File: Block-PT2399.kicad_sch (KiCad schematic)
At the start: 24 parts, among them J1 Sig_in, J2 Sig_out, J3 Sig_gnd, J4 +9V, Q1 2N3819, U1 LM7805_TO220, U2 PT2399

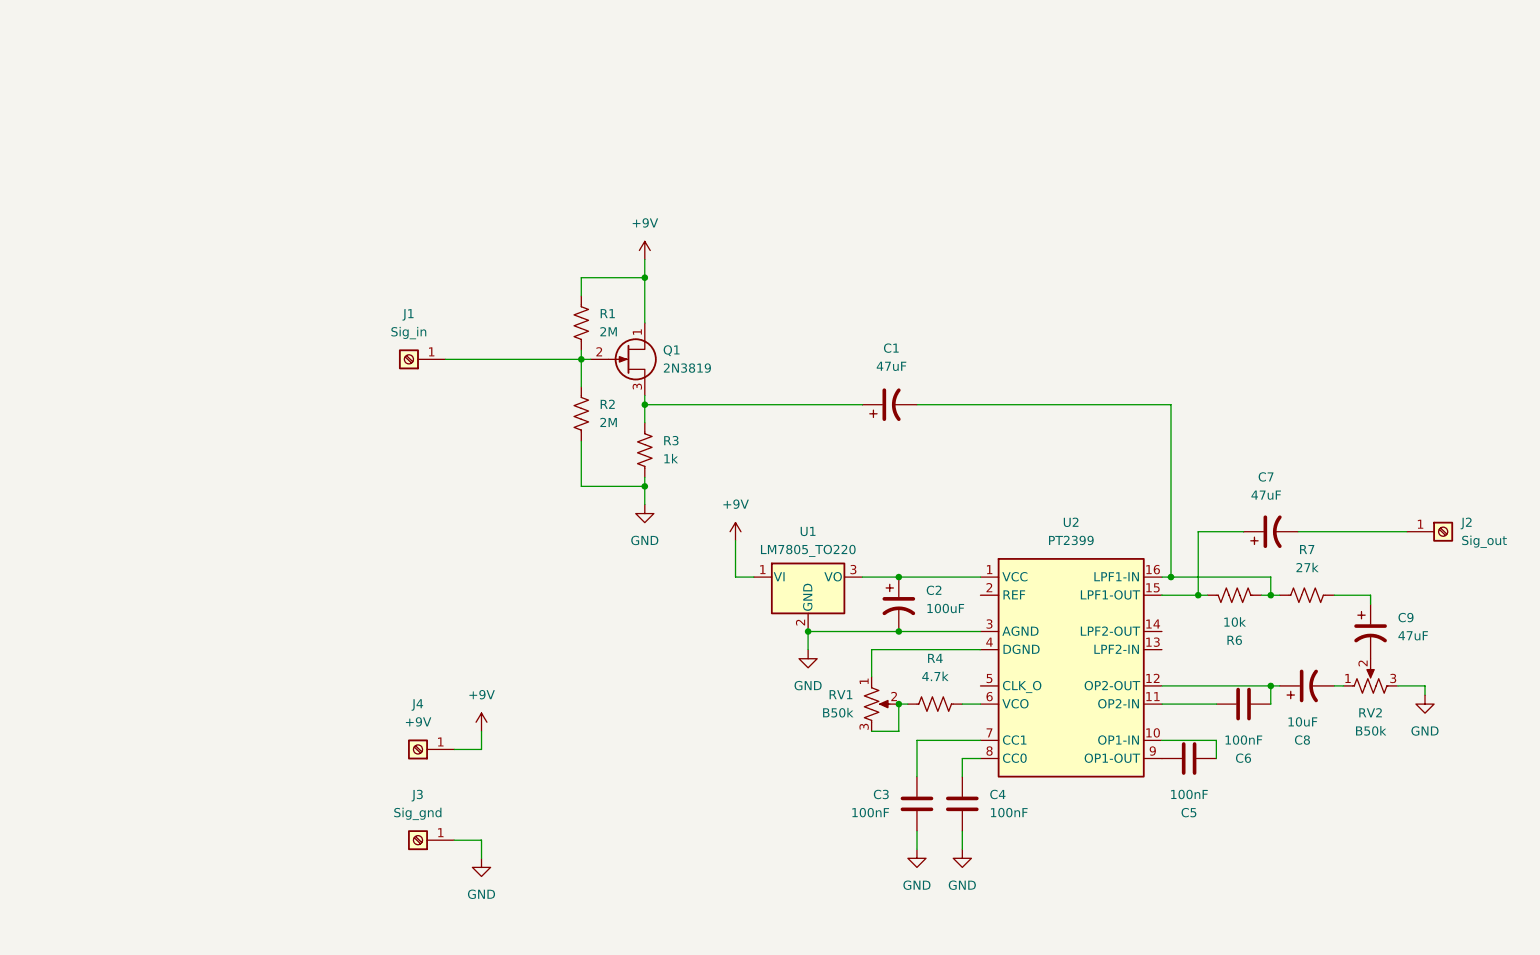
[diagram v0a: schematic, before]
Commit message: implement pin-2 hack and anti-latch
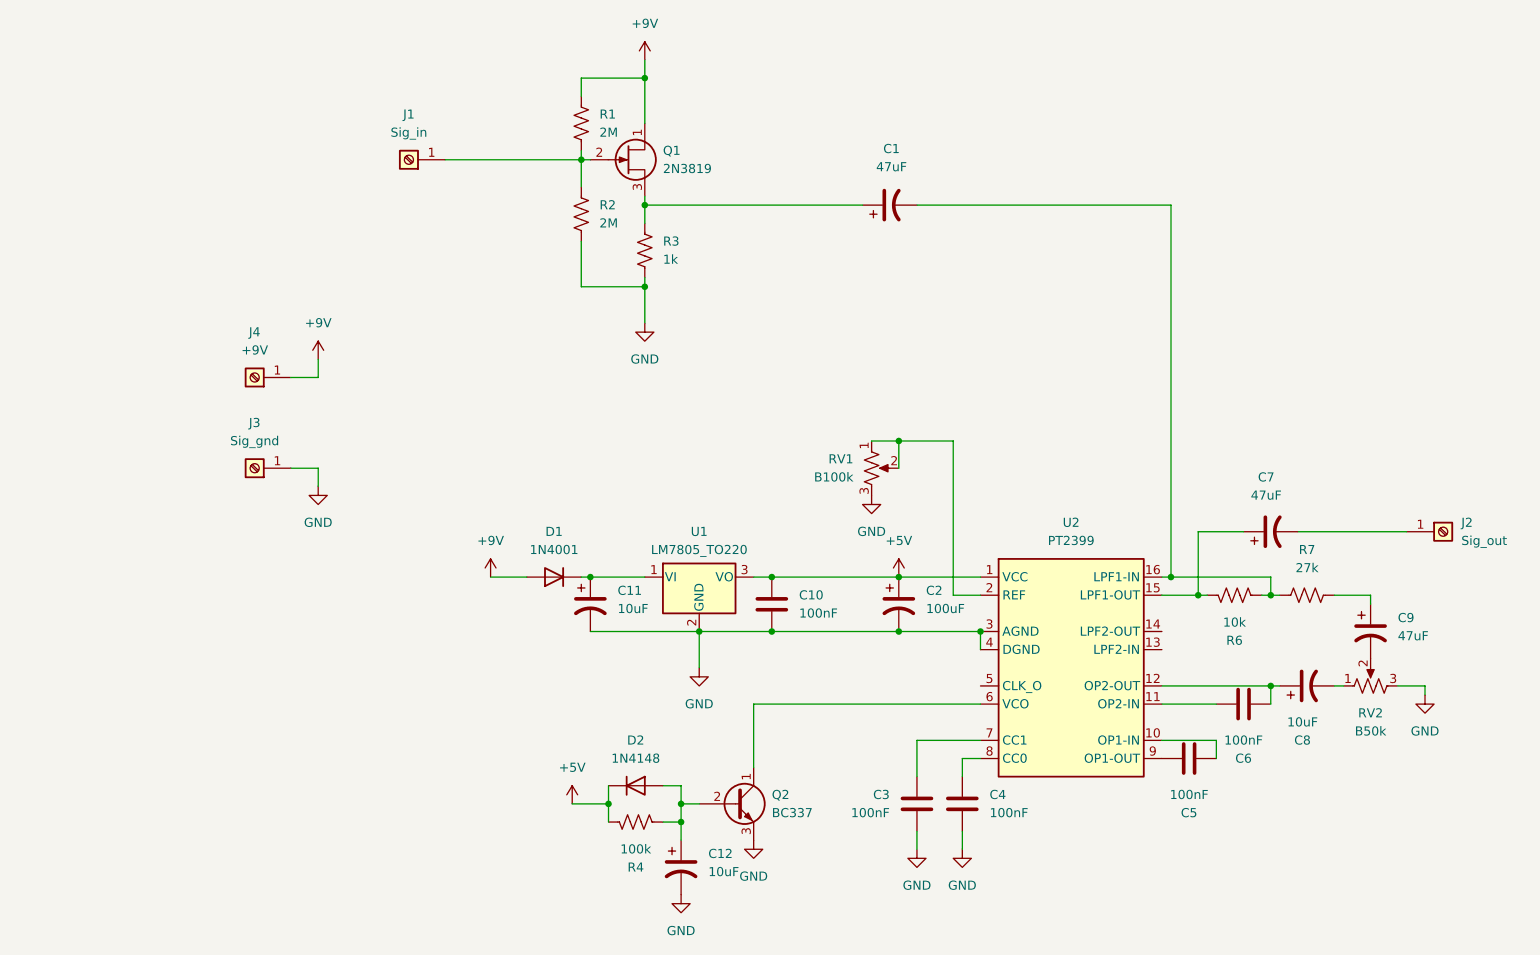
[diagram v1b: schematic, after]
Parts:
- added C10: 100nF, Capacitor_THT:C_Disc_D3.0mm_W1.6mm_P2.50mm, symbol Device:C
- added C11: 10uF, Capacitor_THT:CP_Radial_D5.0mm_P2.00mm, symbol Device:C_Polarized_US
- added C12: 10uF, Capacitor_THT:CP_Radial_D4.0mm_P2.00mm, symbol Device:C_Polarized_US
- added D1: 1N4001, Diode_THT:D_DO-41_SOD81_P10.16mm_Horizontal, symbol Diode:1N4001
- added D2: 1N4148, Diode_THT:D_DO-35_SOD27_P7.62mm_Horizontal, symbol Diode:1N4148
- added Q2: BC337, Package_TO_SOT_THT:TO-92_Inline, symbol Transistor_BJT:BC337
- R4: value 4.7k -> 100k; footprint Resistor_THT:R_Axial_DIN0207_L6.3mm_D2.5mm_P10.16mm_Horizontal -> Resistor_THT:R_Axial_DIN0204_L3.6mm_D1.6mm_P5.08mm_Horizontal
- RV1: value B50k -> B100k
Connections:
- net +9V: now also D1.2 (A); no longer U1.1 (VI)
- net GND: now also RV1.3, U2.4 (DGND), C10.2, C11.2, C12.2, Q2.3 (E)
- net at RV1.1: now also RV1.2, U2.2 (REF); no longer U2.4 (DGND)
- net at U2.6 (VCO): now also Q2.1 (C); no longer R4.2
- net +5V: now reaches C2.1, U1.3 (VO), U2.1 (VCC)
- net +5V: now also R4.2, C10.1, D2.1 (K)
- new net: C11.1, D1.1 (K), U1.1 (VI)
- new net: C12.1, D2.2 (A), Q2.2 (B), R4.1
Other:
- moved on the sheet: C1, J1, J3, J4, Q1, R1, R2, R3, RV1, U1

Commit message: working on redoing board size and layout, dropped the diode
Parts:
- removed D1: 1N4001, Diode_THT:D_DO-41_SOD81_P10.16mm_Horizontal, symbol Diode:1N4001
- added H1, H2, H3, H4: MountingHole, MountingHole:MountingHole_2.2mm_M2, symbol Mechanical:MountingHole
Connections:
- net +9V: now also C11.1, U1.1 (VI)
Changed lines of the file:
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@@
 	(wire
 		(pts
-			(xy 119.38 92.71) (xy 118.11 92.71)
-		)
-		(stroke
-			(width 0)
-			(type default)
-		)
-	)
-	(wire
-		(pts
 			(xy 118.11 52.07) (xy 127 52.07)
 		)
@@
 	(wire
 		(pts
-			(xy 105.41 92.71) (xy 110.49 92.71)
+			(xy 105.41 92.71) (xy 119.38 92.71)
 		)
 		(stroke
@@
 	)
 	(symbol
-		(lib_id "Diode:1N4001")
-		(at 114.3 92.71 180)
-		(unit 1)
-		(exclude_from_sim no)
-		(in_bom yes)
-		(on_board yes)
-		(dnp no)
-		(fields_autoplaced yes)
-		(property "Reference" "D1"
-			(at 114.3 86.36 0)
-			(effects
-				(font
-					(size 1.27 1.27)
-				)
-			)
-		)
-		(property "Value" "1N4001"
-			(at 114.3 88.9 0)
-			(effects
-				(font
-					(size 1.27 1.27)
-				)
-			)
-		)
-		(property "Footprint" "Diode_THT:D_DO-41_SOD81_P10.16mm_Horizontal"
-			(at 114.3 92.71 0)
-			(effects
-				(font
-					(size 1.27 1.27)
-				)
-				(hide yes)
-			)
-		)
-		(property "Datasheet" "http://www.vishay.com/docs/88503/1n4001.pdf"
-			(at 114.3 92.71 0)
-			(effects
-				(font
-					(size 1.27 1.27)
-				)
-				(hide yes)
-			)
-		)
-		(property "Description" "50V 1A General Purpose Rectifier Diode, DO-41"
-			(at 114.3 92.71 0)
-			(effects
-				(font
-					(size 1.27 1.27)
-				)
-				(hide yes)
-			)
-		)
-		(property "Sim.Device" "D"
-			(at 114.3 92.71 0)
-			(effects
-				(font
-					(size 1.27 1.27)
-				)
-				(hide yes)
-			)
-		)
-		(property "Sim.Pins" "1=K 2=A"
-			(at 114.3 92.71 0)
-			(effects
-				(font
-					(size 1.27 1.27)
-				)
-				(hide yes)
-			)
-		)
-		(pin "2"
-		)
-		(pin "1"
-		)
-		(instances
-			(project ""
-				(path "/440b239d-7aa4-4651-bb1c-65d43585ed88"
-					(reference "D1")
-					(unit 1)
-				)
-			)
-		)
-	)
-	(symbol
 		(lib_id "power:GND")
 		(at 132.08 137.16 0)
@@
 	)
 	(symbol
+		(lib_id "Mechanical:MountingHole")
+		(at 40.64 54.61 0)
+		(unit 1)
+		(exclude_from_sim yes)
+		(in_bom no)
+		(on_board yes)
+		(dnp no)
+		(fields_autoplaced yes)
+		(property "Reference" "H3"
+			(at 43.18 53.3399 0)
+			(effects
+				(font
+					(size 1.27 1.27)
+				)
+				(justify left)
+			)
+		)
+		(property "Value" "MountingHole"
+			(at 43.18 55.8799 0)
+			(effects
+				(font
+					(size 1.27 1.27)
+				)
+				(justify left)
+			)
+		)
+		(property "Footprint" "MountingHole:MountingHole_2.2mm_M2"
+			(at 40.64 54.61 0)
+			(effects
+				(font
+					(size 1.27 1.27)
+				)
+				(hide yes)
+			)
+		)
+		(property "Datasheet" "~"
+			(at 40.64 54.61 0)
+			(effects
+				(font
+					(size 1.27 1.27)
+				)
+				(hide yes)
+			)
+		)
+		(property "Description" "Mounting Hole without connection"
+			(at 40.64 54.61 0)
+			(effects
+				(font
+					(size 1.27 1.27)
+				)
+				(hide yes)
+			)
+		)
+		(instances
+			(project "Block-PT2399"
+				(path "/440b239d-7aa4-4651-bb1c-65d43585ed88"
+					(reference "H3")
+					(unit 1)
+				)
+			)
+		)
+	)
+	(symbol
 		(lib_id "power:GND")
 		(at 158.75 81.28 0)
@@
 	)
 	(symbol
+		(lib_id "Mechanical:MountingHole")
+		(at 40.64 62.23 0)
+		(unit 1)
+		(exclude_from_sim yes)
+		(in_bom no)
+		(on_board yes)
+		(dnp no)
+		(fields_autoplaced yes)
+		(property "Reference" "H4"
+			(at 43.18 60.9599 0)
+			(effects
+				(font
+					(size 1.27 1.27)
+				)
+				(justify left)
+			)
+		)
+		(property "Value" "MountingHole"
+			(at 43.18 63.4999 0)
+			(effects
+				(font
+					(size 1.27 1.27)
+				)
+				(justify left)
+			)
+		)
+		(property "Footprint" "MountingHole:MountingHole_2.2mm_M2"
+			(at 40.64 62.23 0)
+			(effects
+				(font
+					(size 1.27 1.27)
+				)
+				(hide yes)
+			)
+		)
+		(property "Datasheet" "~"
+			(at 40.64 62.23 0)
+			(effects
+				(font
+					(size 1.27 1.27)
+				)
+				(hide yes)
+			)
+		)
+		(property "Description" "Mounting Hole without connection"
+			(at 40.64 62.23 0)
+			(effects
+				(font
+					(size 1.27 1.27)
+				)
+				(hide yes)
+			)
+		)
+		(instances
+			(project "Block-PT2399"
+				(path "/440b239d-7aa4-4651-bb1c-65d43585ed88"
+					(reference "H4")
+					(unit 1)
+				)
+			)
+		)
+	)
+	(symbol
+		(lib_id "Mechanical:MountingHole")
+		(at 40.64 39.37 0)
+		(unit 1)
+		(exclude_from_sim yes)
+		(in_bom no)
+		(on_board yes)
+		(dnp no)
+		(fields_autoplaced yes)
+		(property "Reference" "H1"
+			(at 43.18 38.0999 0)
+			(effects
+				(font
+					(size 1.27 1.27)
+				)
+				(justify left)
+			)
+		)
+		(property "Value" "MountingHole"
+			(at 43.18 40.6399 0)
+			(effects
+				(font
+					(size 1.27 1.27)
+				)
+				(justify left)
+			)
+		)
+		(property "Footprint" "MountingHole:MountingHole_2.2mm_M2"
+			(at 40.64 39.37 0)
+			(effects
+				(font
+					(size 1.27 1.27)
+				)
+				(hide yes)
+			)
+		)
+		(property "Datasheet" "~"
+			(at 40.64 39.37 0)
+			(effects
+				(font
+					(size 1.27 1.27)
+				)
+				(hide yes)
+			)
+		)
+		(property "Description" "Mounting Hole without connection"
+			(at 40.64 39.37 0)
+			(effects
+				(font
+					(size 1.27 1.27)
+				)
+				(hide yes)
+			)
+		)
+		(instances
+			(project ""
+				(path "/440b239d-7aa4-4651-bb1c-65d43585ed88"
+					(reference "H1")
+					(unit 1)
+				)
+			)
+		)
+	)
+	(symbol
 		(lib_id "Device:R_US")
 		(at 118.11 41.91 0)
@@
 					(unit 1)
 				)
+			)
+		)
+	)
+	(symbol
+		(lib_id "Mechanical:MountingHole")
+		(at 40.64 46.99 0)
+		(unit 1)
+		(exclude_from_sim yes)
+		(in_bom no)
+		(on_board yes)
+		(dnp no)
+		(fields_autoplaced yes)
+		(property "Reference" "H2"
+			(at 43.18 45.7199 0)
+			(effects
+				(font
+					(size 1.27 1.27)
+				)
+				(justify left)
+			)
+		)
+		(property "Value" "MountingHole"
+			(at 43.18 48.2599 0)
+			(effects
+				(font
+					(size 1.27 1.27)
+				)
+				(justify left)
+			)
+		)
+		(property "Footprint" "MountingHole:MountingHole_2.2mm_M2"
+			(at 40.64 46.99 0)
+			(effects
+				(font
+					(size 1.27 1.27)
+				)
+				(hide yes)
+			)
+		)
+		(property "Datasheet" "~"
+			(at 40.64 46.99 0)
+			(effects
+				(font
+					(size 1.27 1.27)
+				)
+				(hide yes)
+			)
+		)
+		(property "Description" "Mounting Hole without connection"
+			(at 40.64 46.99 0)
+			(effects
+				(font
+					(size 1.27 1.27)
+				)
+				(hide yes)
+			)
+		)
+		(instances
+			(project "Block-PT2399"
+				(path "/440b239d-7aa4-4651-bb1c-65d43585ed88"
+					(reference "H2")
+					(unit 1)
+				)
